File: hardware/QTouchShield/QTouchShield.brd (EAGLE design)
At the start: 100 x 80 mm, 114 parts, among them IC1 AT32UC3C0512CJEDEC-MS-026, U1 ARDUINO-MEGALITE

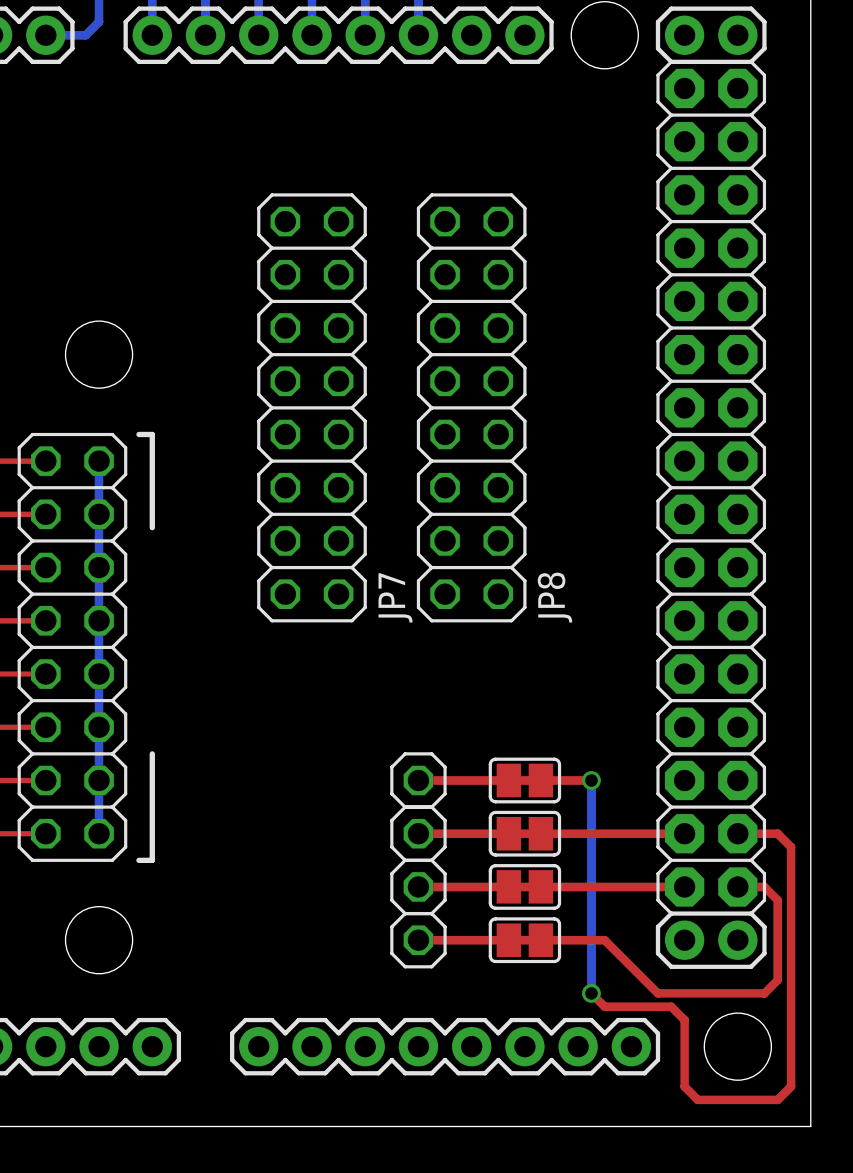
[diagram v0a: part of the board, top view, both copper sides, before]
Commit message: Swapped MISO/MOSI connection to Arduino - wrong way round.
The MISO/MOSI lines from the UC3C to the Arduino were swapped.
Fixed in the schematic and board.
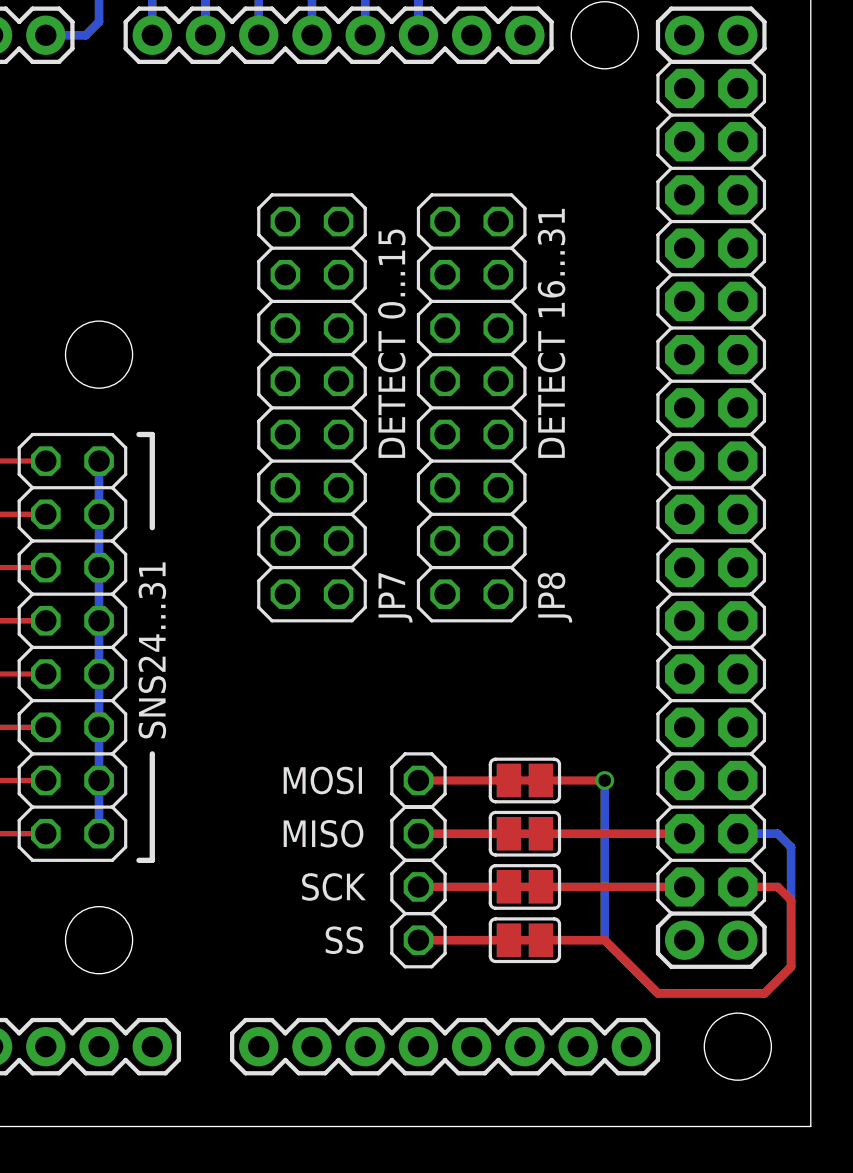
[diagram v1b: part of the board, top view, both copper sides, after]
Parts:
- moved JP12 2.54 mm to (81.3, 14.0)
- moved JP13 2.54 mm to (81.3, 16.5)
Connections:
- net SDT-SPI0-MISO: now also SJ4.1, SJ4.2, U1.50; no longer SJ3.1, SJ3.2, U1.51
- net SDT-SPI0-MOSI: now also SJ3.1, SJ3.2, U1.51; no longer SJ4.1, SJ4.2, U1.50
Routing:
- net SDT-SPI0-MISO: track 46.4 -> 12.7 mm, vias 2 -> 0
- net SDT-SPI0-MOSI: track 12.7 -> 35.5 mm, vias 0 -> 1
- net SDT-SPI0-SS: track 24.4 -> 25.3 mm
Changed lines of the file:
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@@
 </element>
 <element name="JP5" library="pinhead" package="2X08" value="SNS24...31" x="64.77" y="22.86" smashed="yes" rot="R90">
-<attribute name="VALUE" x="69.215" y="18.415" size="1.27" layer="27" rot="R90"/>
+<attribute name="VALUE" x="69.215" y="18.415" size="1.27" layer="21" rot="R90"/>
 </element>
 <element name="R17" library="SparkFun" package="0805" value="1K" x="8.89" y="62.23"/>
@@
 <element name="LED1" library="SparkFun" package="LED-1206" value="Yellow" x="81.28" y="67.31"/>
 <element name="JP8" library="pinhead" package="2X08" value="DETECT 16...31" x="83.82" y="34.29" smashed="yes" rot="R270">
-<attribute name="NAME" x="88.265" y="24.13" size="1.27" layer="25" ratio="10" rot="R90"/>
-<attribute name="VALUE" x="88.265" y="31.75" size="1.27" layer="27" rot="R90"/>
+<attribute name="NAME" x="88.265" y="24.13" size="1.27" layer="21" ratio="10" rot="R90"/>
+<attribute name="VALUE" x="88.265" y="31.75" size="1.27" layer="21" rot="R90"/>
 </element>
 <element name="JP7" library="pinhead" package="2X08" value="DETECT 0...15" x="76.2" y="34.29" smashed="yes" rot="R270">
-<attribute name="NAME" x="80.645" y="24.13" size="1.27" layer="25" ratio="10" rot="R90"/>
-<attribute name="VALUE" x="80.645" y="31.75" size="1.27" layer="27" rot="R90"/>
+<attribute name="NAME" x="80.645" y="24.13" size="1.27" layer="21" ratio="10" rot="R90"/>
+<attribute name="VALUE" x="80.645" y="31.75" size="1.27" layer="21" rot="R90"/>
 </element>
 <element name="JP9" library="pinhead" package="2X08" value="COMMS Select" x="72.39" y="58.42"/>
@@
 </element>
 <element name="JP10" library="pinhead" package="1X01" value="SS" x="81.28" y="8.89" smashed="yes" rot="R270">
-<attribute name="VALUE" x="78.74" y="9.525" size="1.27" layer="27" font="vector" rot="R180"/>
+<attribute name="VALUE" x="78.74" y="9.525" size="1.27" layer="21" font="vector" rot="R180"/>
 </element>
 <element name="JP11" library="pinhead" package="1X01" value="SCK" x="81.28" y="11.43" smashed="yes" rot="R270">
-<attribute name="VALUE" x="78.74" y="12.065" size="1.27" layer="27" font="vector" rot="R180"/>
+<attribute name="VALUE" x="78.74" y="12.065" size="1.27" layer="21" font="vector" rot="R180"/>
 </element>
-<element name="JP12" library="pinhead" package="1X01" value="MISO" x="81.28" y="16.51" smashed="yes" rot="R270">
-<attribute name="VALUE" x="78.74" y="17.145" size="1.27" layer="27" font="vector" rot="R180"/>
+<element name="JP12" library="pinhead" package="1X01" value="MISO" x="81.28" y="13.97" smashed="yes" rot="R270">
+<attribute name="VALUE" x="78.74" y="14.605" size="1.27" layer="21" font="vector" rot="R180"/>
 </element>
-<element name="JP13" library="pinhead" package="1X01" value="MOSI" x="81.28" y="13.97" smashed="yes" rot="R270">
-<attribute name="VALUE" x="78.74" y="14.605" size="1.27" layer="27" font="vector" rot="R180"/>
+<element name="JP13" library="pinhead" package="1X01" value="MOSI" x="81.28" y="16.51" smashed="yes" rot="R270">
+<attribute name="VALUE" x="78.74" y="17.145" size="1.27" layer="21" font="vector" rot="R180"/>
 </element>
 <element name="JP14" library="pinhead" package="1X01" value="SCK" x="29.21" y="55.88" smashed="yes">
@@
 <contactref element="U1" pad="53"/>
 <contactref element="SJ1" pad="1"/>
+<wire x1="85.598" y1="8.89" x2="87.122" y2="8.89" width="0.4064" layer="1"/>
+<wire x1="96.52" y1="11.43" x2="97.79" y2="11.43" width="0.4064" layer="1"/>
+<wire x1="97.79" y1="11.43" x2="98.425" y2="11.43" width="0.4064" layer="1"/>
+<wire x1="98.425" y1="11.43" x2="99.06" y2="10.795" width="0.4064" layer="1"/>
+<wire x1="99.06" y1="10.795" x2="99.06" y2="7.62" width="0.4064" layer="1"/>
+<wire x1="99.06" y1="7.62" x2="97.79" y2="6.35" width="0.4064" layer="1"/>
+<wire x1="97.79" y1="6.35" x2="92.71" y2="6.35" width="0.4064" layer="1"/>
+<wire x1="92.71" y1="6.35" x2="90.805" y2="8.255" width="0.4064" layer="1"/>
+<wire x1="90.805" y1="8.255" x2="90.17" y2="8.89" width="0.4064" layer="1"/>
 <wire x1="90.17" y1="8.89" x2="87.122" y2="8.89" width="0.4064" layer="1"/>
-<wire x1="96.52" y1="11.43" x2="97.79" y2="11.43" width="0.4064" layer="1"/>
-<wire x1="97.79" y1="6.35" x2="92.71" y2="6.35" width="0.4064" layer="1"/>
-<wire x1="92.71" y1="6.35" x2="90.17" y2="8.89" width="0.4064" layer="1"/>
-<wire x1="97.79" y1="11.43" x2="98.425" y2="10.795" width="0.4064" layer="1"/>
-<wire x1="98.425" y1="10.795" x2="98.425" y2="6.985" width="0.4064" layer="1"/>
-<wire x1="98.425" y1="6.985" x2="97.79" y2="6.35" width="0.4064" layer="1"/>
-<wire x1="85.598" y1="8.89" x2="87.122" y2="8.89" width="0.4064" layer="1"/>
 <wire x1="45.715" y1="39.175" x2="81.28" y2="8.89" width="0" layer="19" extent="1-1"/>
 </signal>
 <signal name="SDT-SPI0-MOSI">
 <contactref element="IC1" pad="111"/>
-<contactref element="SJ4" pad="2"/>
+<contactref element="SJ3" pad="2"/>
+<contactref element="SJ3" pad="1"/>
+<wire x1="85.598" y1="16.51" x2="87.122" y2="16.51" width="0.4064" layer="1"/>
+<contactref element="U1" pad="51"/>
 <contactref element="JP13" pad="1"/>
-<wire x1="81.28" y1="13.97" x2="85.598" y2="13.97" width="0.4064" layer="1"/>
-<contactref element="U1" pad="50"/>
-<contactref element="SJ4" pad="1"/>
-<wire x1="93.98" y1="13.97" x2="87.122" y2="13.97" width="0.4064" layer="1"/>
-<wire x1="85.598" y1="13.97" x2="87.122" y2="13.97" width="0.4064" layer="1"/>
-<wire x1="45.215" y1="39.175" x2="81.28" y2="13.97" width="0" layer="19" extent="1-1"/>
+<wire x1="96.52" y1="13.97" x2="98.425" y2="13.97" width="0.4064" layer="16"/>
+<wire x1="98.425" y1="13.97" x2="99.06" y2="13.335" width="0.4064" layer="16"/>
+<wire x1="99.06" y1="13.335" x2="99.06" y2="7.62" width="0.4064" layer="16"/>
+<wire x1="99.06" y1="7.62" x2="97.79" y2="6.35" width="0.4064" layer="16"/>
+<wire x1="97.79" y1="6.35" x2="92.71" y2="6.35" width="0.4064" layer="16"/>
+<wire x1="92.71" y1="6.35" x2="90.17" y2="8.89" width="0.4064" layer="16"/>
+<wire x1="90.17" y1="8.89" x2="90.17" y2="16.51" width="0.4064" layer="16"/>
+<via x="90.17" y="16.51" extent="1-16" drill="0.6" shape="square"/>
+<wire x1="90.17" y1="16.51" x2="87.122" y2="16.51" width="0.4064" layer="1"/>
+<wire x1="81.28" y1="16.51" x2="85.598" y2="16.51" width="0.4064" layer="1"/>
+<wire x1="45.215" y1="39.175" x2="81.28" y2="16.51" width="0" layer="19" extent="1-1"/>
 </signal>
 <signal name="SDT-SPI0-MISO">
 <contactref element="IC1" pad="112"/>
-<contactref element="SJ3" pad="2"/>
+<contactref element="SJ4" pad="2"/>
+<contactref element="SJ4" pad="1"/>
+<wire x1="85.598" y1="13.97" x2="87.122" y2="13.97" width="0.4064" layer="1"/>
+<contactref element="U1" pad="50"/>
 <contactref element="JP12" pad="1"/>
-<wire x1="85.598" y1="16.51" x2="81.28" y2="16.51" width="0.4064" layer="1"/>
-<contactref element="U1" pad="51"/>
-<contactref element="SJ3" pad="1"/>
-<wire x1="96.52" y1="13.97" x2="98.425" y2="13.97" width="0.4064" layer="1"/>
-<wire x1="98.425" y1="13.97" x2="99.06" y2="13.335" width="0.4064" layer="1"/>
-<wire x1="99.06" y1="13.335" x2="99.06" y2="1.905" width="0.4064" layer="1"/>
-<wire x1="99.06" y1="1.905" x2="98.425" y2="1.27" width="0.4064" layer="1"/>
-<wire x1="98.425" y1="1.27" x2="94.615" y2="1.27" width="0.4064" layer="1"/>
-<wire x1="94.615" y1="1.27" x2="93.98" y2="1.905" width="0.4064" layer="1"/>
-<wire x1="93.98" y1="1.905" x2="93.98" y2="5.08" width="0.4064" layer="1"/>
-<wire x1="93.98" y1="5.08" x2="93.345" y2="5.715" width="0.4064" layer="1"/>
-<wire x1="93.345" y1="5.715" x2="90.17" y2="5.715" width="0.4064" layer="1"/>
-<wire x1="90.17" y1="5.715" x2="89.535" y2="6.35" width="0.4064" layer="1"/>
-<via x="89.535" y="6.35" extent="1-16" drill="0.6" shape="square"/>
-<wire x1="89.535" y1="6.35" x2="89.535" y2="16.51" width="0.4064" layer="16"/>
-<via x="89.535" y="16.51" extent="1-16" drill="0.6" shape="square"/>
-<wire x1="89.535" y1="16.51" x2="87.122" y2="16.51" width="0.4064" layer="1"/>
-<wire x1="85.598" y1="16.51" x2="87.122" y2="16.51" width="0.4064" layer="1"/>
-<wire x1="44.715" y1="39.175" x2="81.28" y2="16.51" width="0" layer="19" extent="1-1"/>
+<wire x1="81.28" y1="13.97" x2="85.598" y2="13.97" width="0.4064" layer="1"/>
+<wire x1="87.122" y1="13.97" x2="93.98" y2="13.97" width="0.4064" layer="1"/>
+<wire x1="44.715" y1="39.175" x2="81.28" y2="13.97" width="0" layer="19" extent="1-1"/>
 </signal>
 <signal name="SDT-SPI0-SCK">

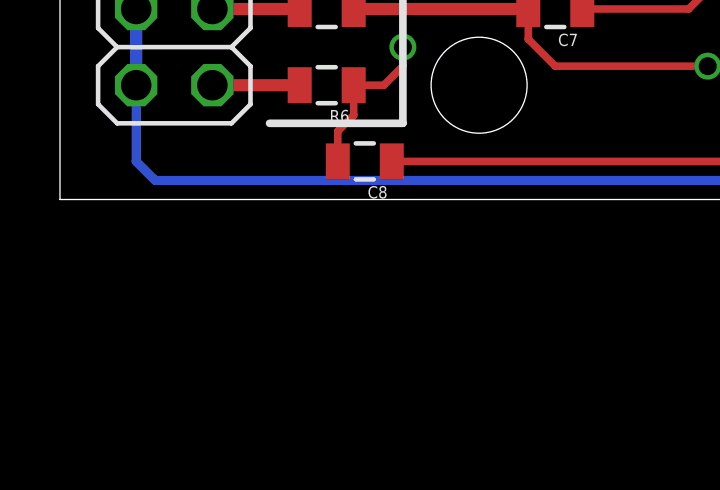
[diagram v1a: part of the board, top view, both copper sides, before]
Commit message: Added TOUCH DATA header for data transfer to QT600 Interface Board
TOUCH DATA header added. This is the bit-banged SPI interface for
transferring debug data to the QT600 board for analysing touch data
with QTouch Studio.
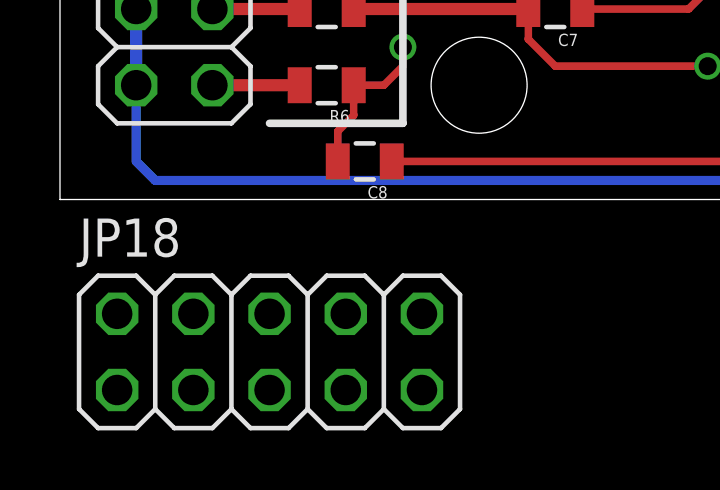
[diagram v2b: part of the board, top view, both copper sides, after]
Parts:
- added JP18: TOUCH DATA, pinhead:2X05
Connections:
- new net TOUCH_DATA-MISO: IC1.133, JP18.7
- new net TOUCH_DATA-MOSI: IC1.132, JP18.6
- new net TOUCH_DATA-SCK: IC1.131, JP18.8
- new net TOUCH_DATA-SS: IC1.130, JP18.5
- net GND: now also JP18.9
- net VCC: now also JP18.10
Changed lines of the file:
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@@
 <element name="R35" library="SparkFun" package="0805" value="10K" x="73.66" y="74.93" rot="R90"/>
 <element name="SJ5" library="jumper" package="SJ" value="RESET-LINK" x="68.58" y="74.93" rot="R90"/>
+<element name="JP18" library="pinhead" package="2X05" value="TOUCH DATA" x="6.985" y="-5.08"/>
 </elements>
 <signals>
@@
 <wire x1="84.455" y1="79.375" x2="85.09" y2="78.74" width="0.4064" layer="16"/>
 <wire x1="85.09" y1="78.74" x2="85.09" y2="76.835" width="0.4064" layer="16"/>
+<contactref element="JP18" pad="9"/>
 <wire x1="57.785" y1="78.74" x2="58.05" y2="76.2" width="0" layer="19" extent="1-16"/>
 <wire x1="51.7" y1="76.2" x2="58.05" y2="76.2" width="0" layer="19" extent="1-1"/>
@@
 <wire x1="5.41" y1="73.66" x2="5.41" y2="76.2" width="0" layer="19" extent="1-1"/>
 <wire x1="2.54" y1="62.23" x2="5.41" y2="73.66" width="0" layer="19" extent="1-1"/>
+<wire x1="12.065" y1="-6.35" x2="3.175" y2="0.635" width="0" layer="19" extent="16-16"/>
 <wire x1="38.215" y1="17.975" x2="40.64" y2="3.81" width="0" layer="19" extent="1-1"/>
 <wire x1="36.215" y1="17.975" x2="38.215" y2="17.975" width="0" layer="19" extent="1-1"/>
@@
 <contactref element="IC1" pad="5"/>
 <contactref element="R35" pad="1"/>
+<contactref element="JP18" pad="10"/>
 <wire x1="73.66" y1="74.03" x2="96.52" y2="71.12" width="0" layer="19" extent="1-1"/>
 <wire x1="56.25" y1="76.2" x2="73.66" y2="74.03" width="0" layer="19" extent="1-1"/>
@@
 <wire x1="38.1" y1="3.81" x2="36.715" y2="17.975" width="0" layer="19" extent="1-1"/>
 <wire x1="26.865" y1="35.325" x2="41.715" y2="39.175" width="0" layer="19" extent="1-1"/>
+<wire x1="12.065" y1="-3.81" x2="38.1" y2="3.81" width="0" layer="19" extent="1-1"/>
 </signal>
 <signal name="JTAG_TMS">
@@
 <wire x1="36.83" y1="53.975" x2="36.83" y2="55.88" width="0.4064" layer="16"/>
 </signal>
+<signal name="TOUCH_DATA-SS">
+<contactref element="IC1" pad="130"/>
+<contactref element="JP18" pad="5"/>
+<wire x1="6.985" y1="-6.35" x2="35.715" y2="39.175" width="0" layer="19" extent="1-1"/>
+</signal>
+<signal name="TOUCH_DATA-SCK">
+<contactref element="IC1" pad="131"/>
+<contactref element="JP18" pad="8"/>
+<wire x1="9.525" y1="-3.81" x2="35.215" y2="39.175" width="0" layer="19" extent="1-1"/>
+</signal>
+<signal name="TOUCH_DATA-MOSI">
+<contactref element="IC1" pad="132"/>
+<contactref element="JP18" pad="6"/>
+<wire x1="6.985" y1="-3.81" x2="34.715" y2="39.175" width="0" layer="19" extent="1-1"/>
+</signal>
+<signal name="TOUCH_DATA-MISO">
+<contactref element="IC1" pad="133"/>
+<contactref element="JP18" pad="7"/>
+<wire x1="9.525" y1="-6.35" x2="34.215" y2="39.175" width="0" layer="19" extent="1-1"/>
+</signal>
 </signals>
